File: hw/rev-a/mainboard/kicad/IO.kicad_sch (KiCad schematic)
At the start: 6 parts, among them U11 W65C21N, U12 W65C21N, U13 W65C22N

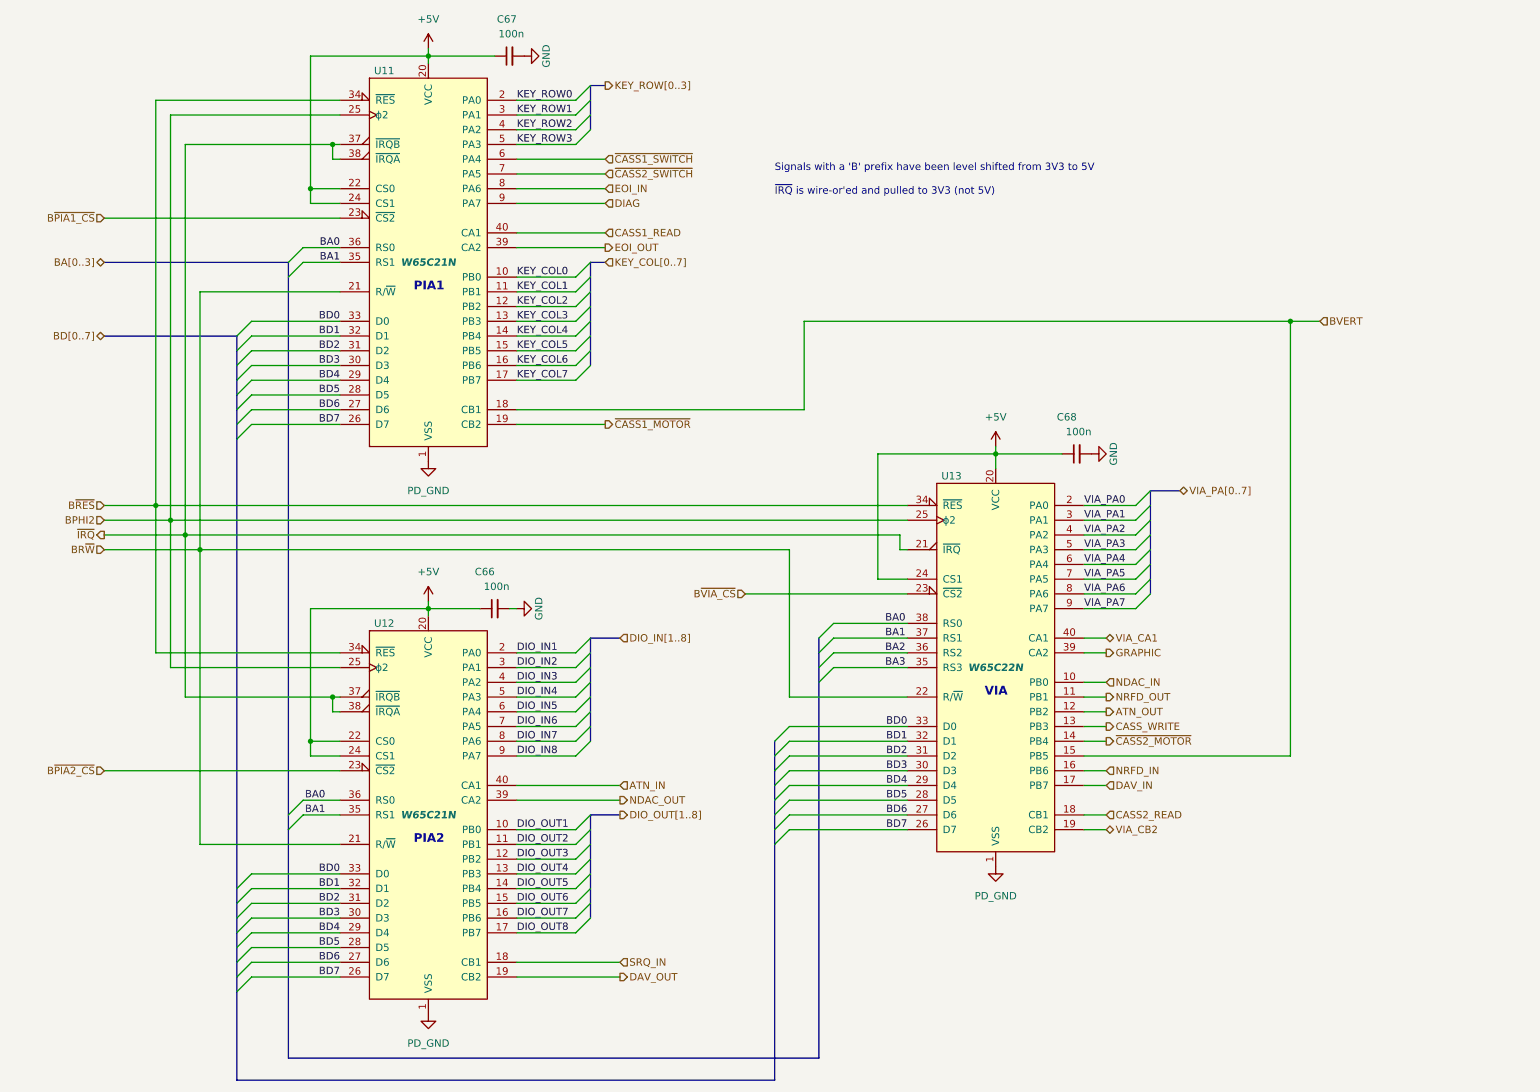
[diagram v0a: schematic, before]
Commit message: hw: ren rev-c -> rev-a
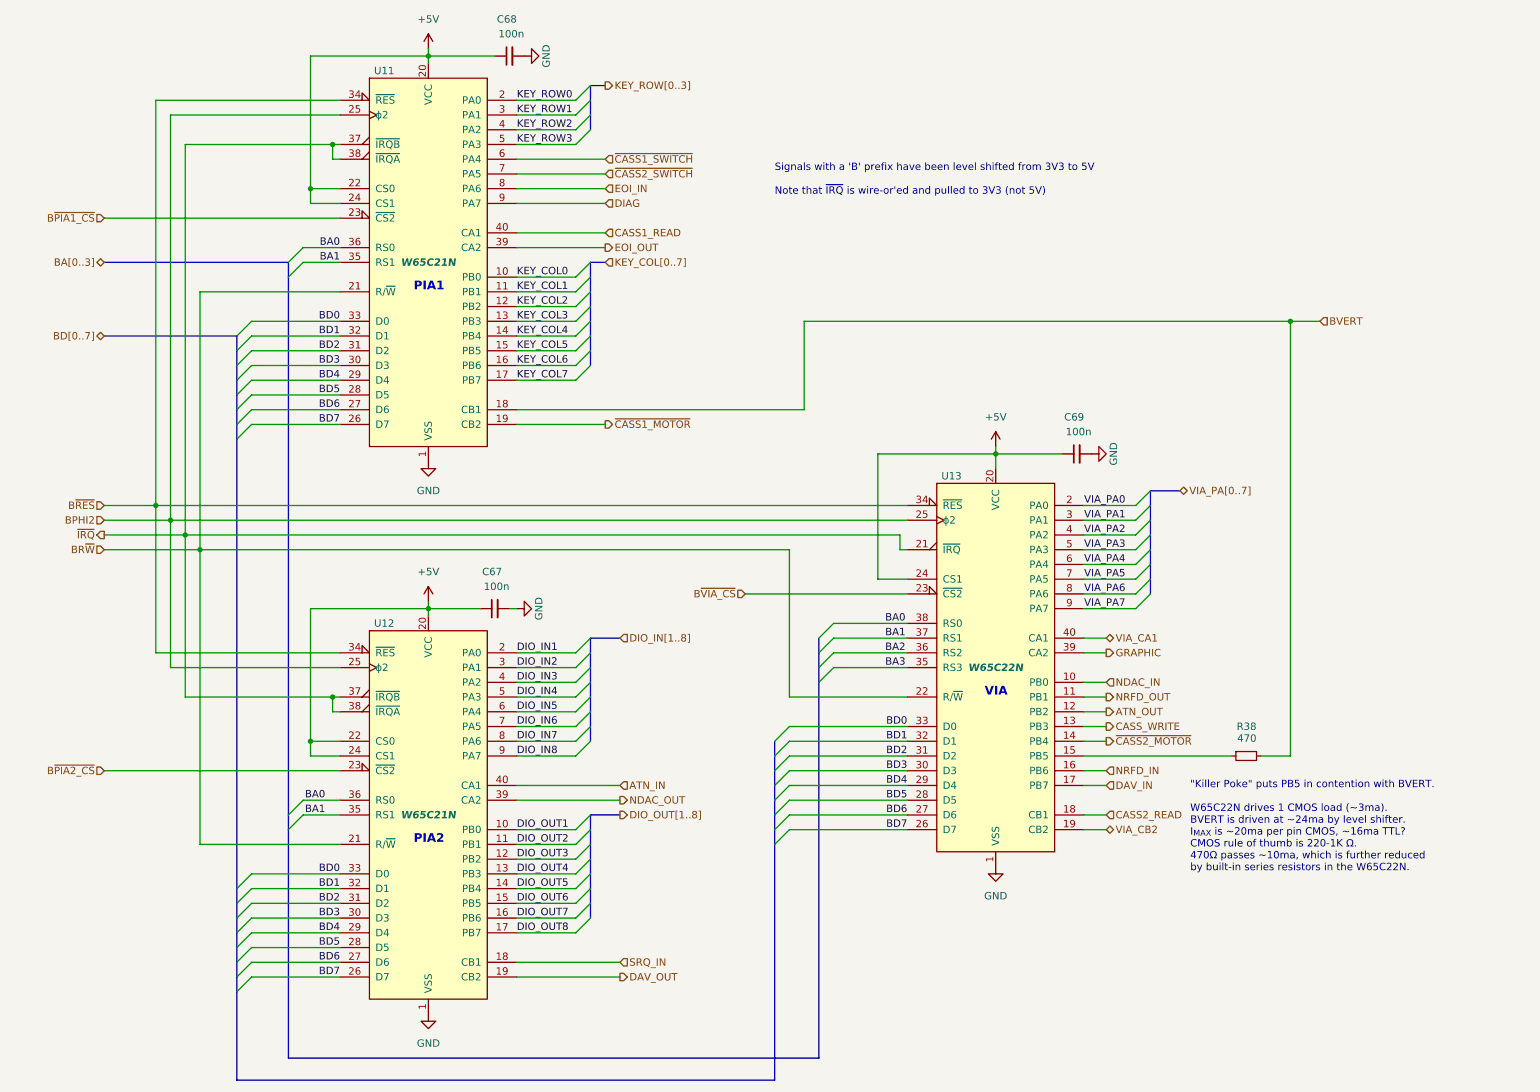
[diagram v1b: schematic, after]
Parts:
- added R38: 470, Resistor_SMD:R_0402_1005Metric, symbol Device:R_Small
- U11, U12: symbol Mainboard-rescue:W65C21NxP-PET -> EconoPET:W65C21N
- U13: symbol Mainboard-rescue:W65C22NxP-PET -> EconoPET:W65C22N
- renumbered C66 to C67, C67 to C68, C68 to C69
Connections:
- net PD_GND is gone; now on net GND: U11.1 (VSS), U12.1 (VSS), U13.1 (VSS)
- net BVERT: now also R38.2; no longer U13.15 (PB5)
- new net: R38.1, U13.15 (PB5)
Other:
- note added: ""Killer Poke" puts PB5 in contention with BVERT. W65C22N drives 1 CMOS load (~3ma). BVERT is driven at ~24ma by level shifter. I_{MAX} is ~20ma per pin CMOS, ~16ma TTL? CMOS rule of thumb is 220-1K Ω. 470Ω passes ~10ma, which is further reduced by built-in series resistors in the W65C22N."
- note added: "Signals with a 'B' prefix have been level shifted from 3V3 to 5V Note that ~{IRQ} is wire-or'ed and pulled to 3V3 (not 5V)"
- note removed: "Signals with a 'B' prefix have been level shifted from 3V3 to 5V ~{IRQ} is wire-or'ed and pulled to 3V3 (not 5V)"

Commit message: hw: tidy schematics for publication
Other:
- note added: "470R protects VIA from "Killer Poke", which puts PB5 in contention with BVERT. W65C22N drives 1 CMOS load (~3ma). BVERT is driven at ~24ma by level shifter. (BVERT easily wins against VIA.)"
- note added: "Note that ~{IRQ} is wire-or'ed and pulled to 3V3 (not 5V)"
- note removed: ""Killer Poke" puts PB5 in contention with BVERT. W65C22N drives 1 CMOS load (~3ma). BVERT is driven at ~24ma by level shifter. I_{MAX} is ~20ma per pin CMOS, ~16ma TTL? CMOS rule of thumb is 220-1K Ω. 470Ω passes ~10ma, which is further reduced by built-in series resistors in the W65C22N."
- note removed: "Signals with a 'B' prefix have been level shifted from 3V3 to 5V Note that ~{IRQ} is wire-or'ed and pulled to 3V3 (not 5V)"
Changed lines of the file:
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@@
 		(date "2023-10-01")
 		(rev "A")
+		(comment 1 "Unspecified resistors are 1% and rated for 62.5mW or higher")
+		(comment 2 "Unspecified capacitors are rated for 25V or higher")
+		(comment 3 "Signals with B-prefix are level-shifted from 3V3 to 5V")
 	)
 	(junction
@@
 		)
 	)
-	(text "\"Killer Poke\" puts PB5 in contention with BVERT.\n\nW65C22N drives 1 CMOS load (~3ma).\nBVERT is driven at ~24ma by level shifter.\nI_{MAX} is ~20ma per pin CMOS, ~16ma TTL?\nCMOS rule of thumb is 220-1K Ω.\n470Ω passes ~10ma, which is further reduced\nby built-in series resistors in the W65C22N."
+	(text "470R protects VIA from \"Killer Poke\", which\nputs PB5 in contention with BVERT.\n\nW65C22N drives 1 CMOS load (~3ma).\nBVERT is driven at ~24ma by level shifter.\n(BVERT easily wins against VIA.)\n"
 		(exclude_from_sim no)
-		(at 217.678 155.702 0)
+		(at 219.71 153.67 0)
 		(effects
 			(font
@@
 		)
 	)
-	(text "Signals with a 'B' prefix have been level shifted from 3V3 to 5V\n\nNote that ~{IRQ} is wire-or'ed and pulled to 3V3 (not 5V)"
+	(text "Note that ~{IRQ} is\nwire-or'ed and pulled\nto 3V3 (not 5V)"
 		(exclude_from_sim no)
-		(at 146.05 46.99 0)
+		(at 15.24 118.11 0)
 		(effects
 			(font

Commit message: hw: tidy schematics for publication
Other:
- company: (none) -> https://is.gd/6hpvh6
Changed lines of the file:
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@@
 		(date "2023-10-01")
 		(rev "A")
-		(comment 1 "Unspecified resistors are 1% and rated for 62.5mW or higher")
-		(comment 2 "Unspecified capacitors are rated for 25V or higher")
+		(company "https://is.gd/6hpvh6")
+		(comment 1 "Unspecified resistors are 1% / 62.5mW")
+		(comment 2 "Unspecified capacitors are 25V")
 		(comment 3 "Signals with B-prefix are level-shifted from 3V3 to 5V")
+		(comment 4 "License: CC0 1.0 Universal (Public Domain Dedication)")
 	)
 	(junction
